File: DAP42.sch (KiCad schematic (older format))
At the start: 30 parts, among them J1 JTAG, J2 Target JTAG, J3 USB_B, Q1 AO3401, SW1 WKUP, U1 W25Q128FV, U2 STM32F042K6Tx, U3 LM1117-3.3, Y1 8MHz

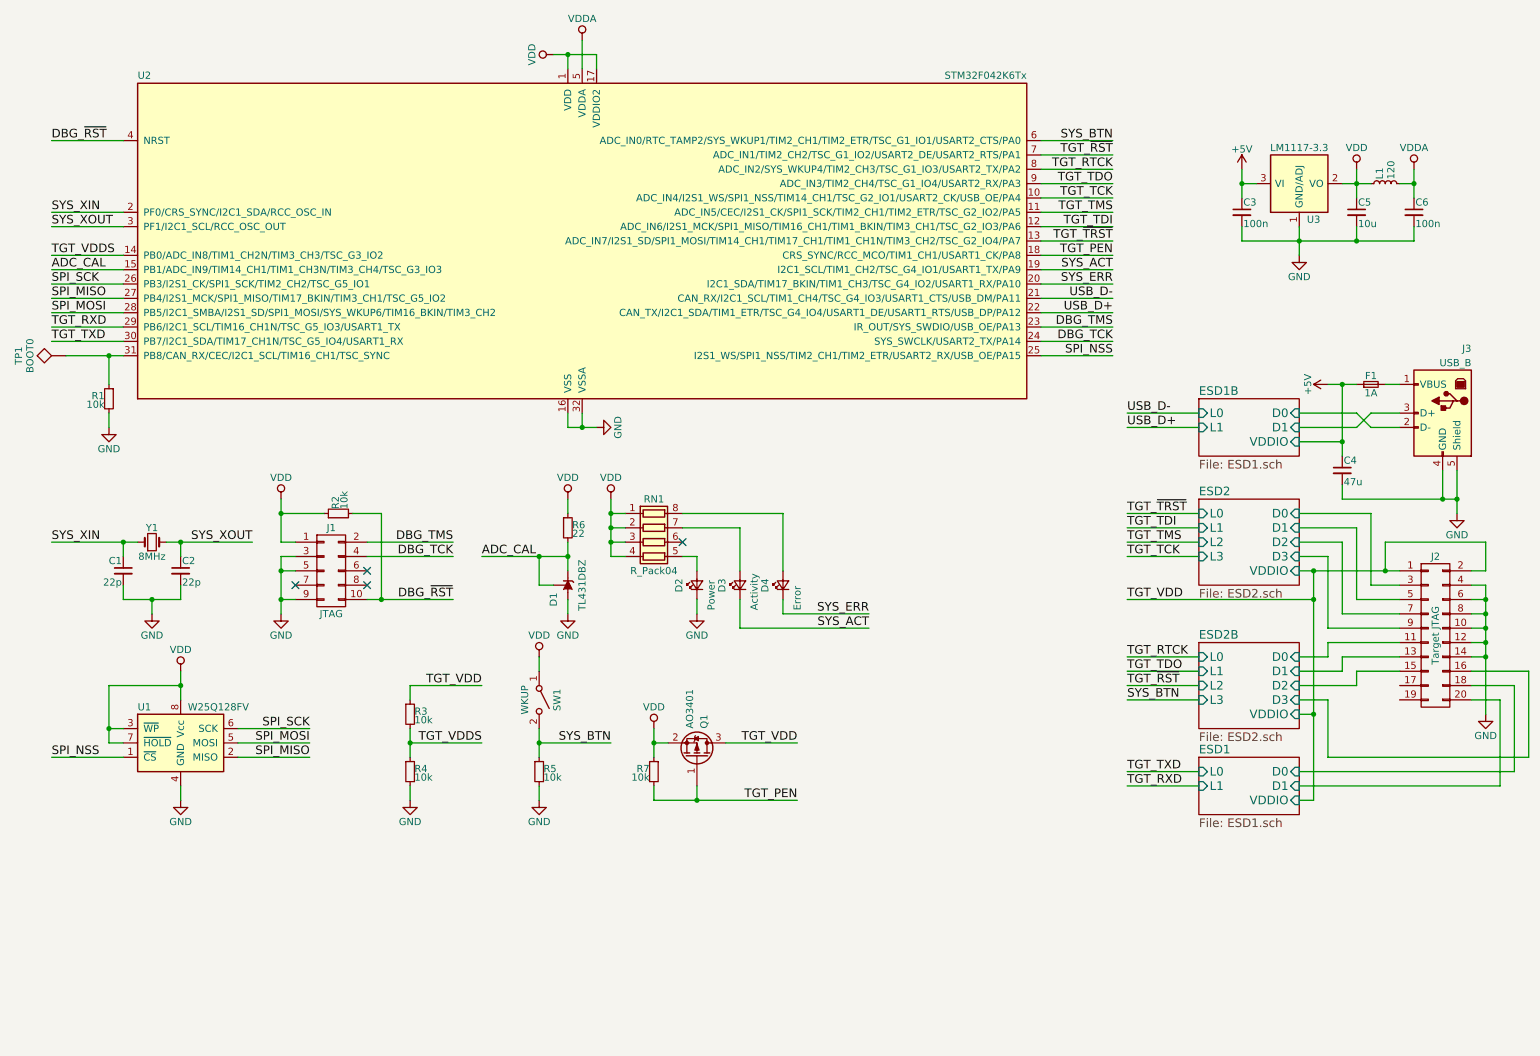
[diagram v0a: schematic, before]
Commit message: Changing the power delivery subsystem.
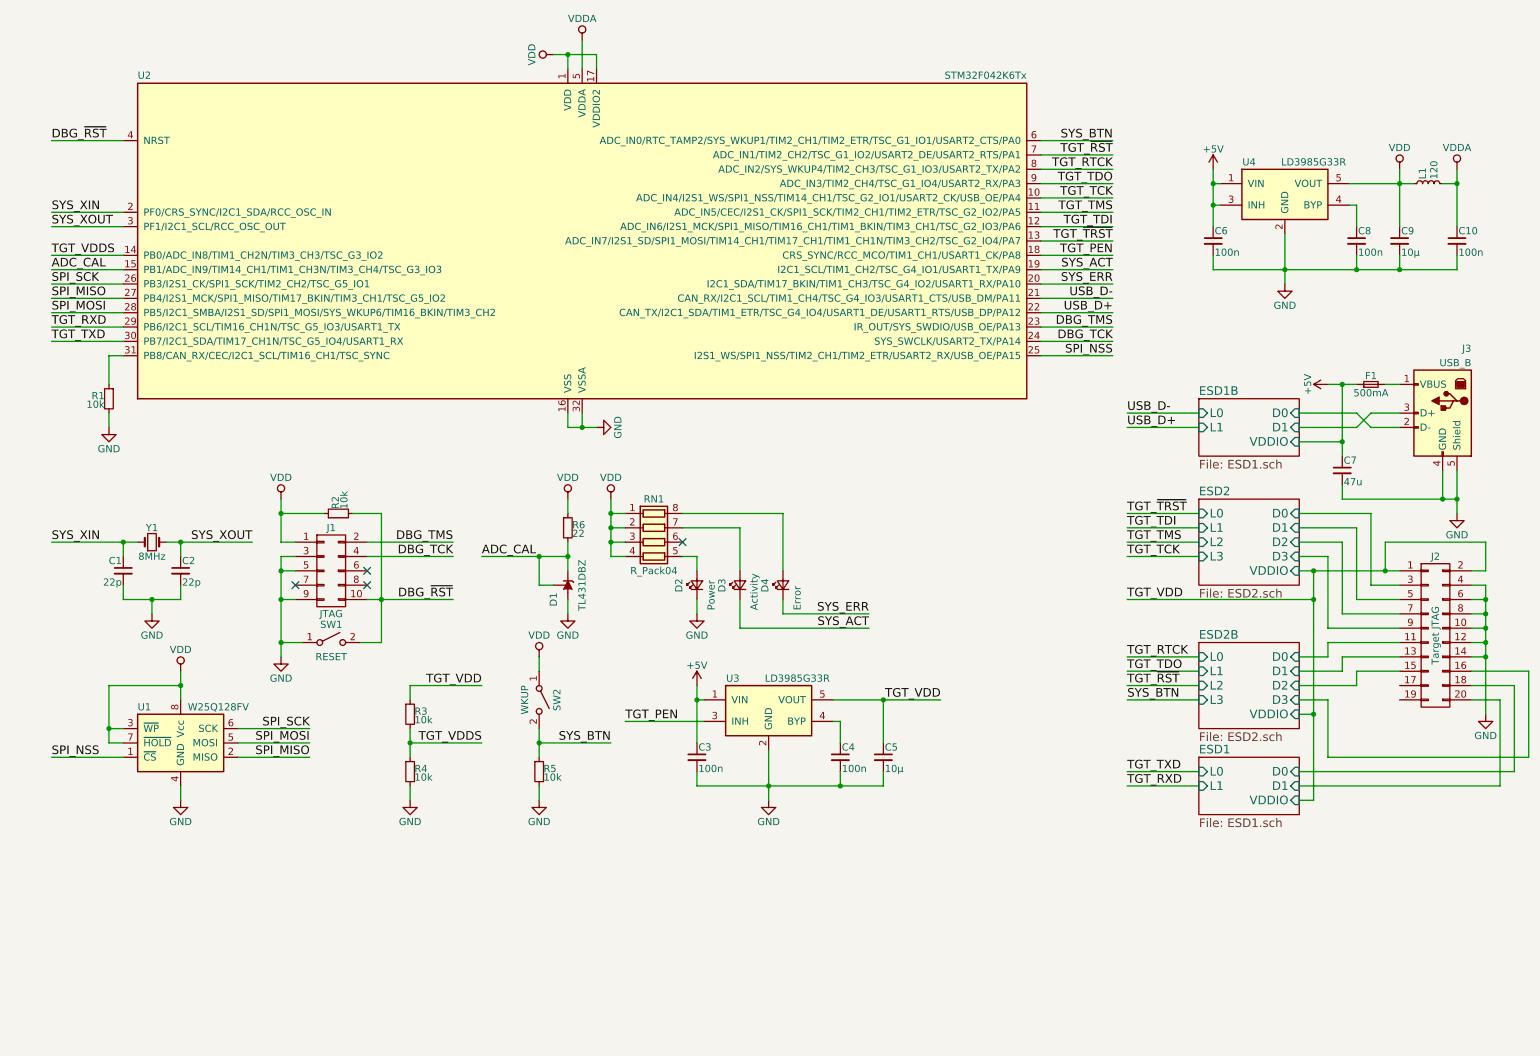
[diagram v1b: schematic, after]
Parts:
- removed Q1: AO3401, TO_SOT_Packages_SMD:SOT-23_Handsoldering, symbol Q_PMOS_GSD
- removed R7: 10k, Resistors_SMD:R_0603_HandSoldering, symbol R_Small
- removed TP1: BOOT0, SMD_Packages:1Pin, symbol TEST
- removed U3: LM1117-3.3, TO_SOT_Packages_SMD:SOT-223, symbol LM1117-3.3
- added C3, C4, C8: 100n, Capacitors_SMD:C_0603_HandSoldering, symbol C_Small
- added C5: 10µ, Capacitors_SMD:C_0805_HandSoldering, symbol C_Small
- added SW1: RESET, Buttons_Switches_SMD:SW_SPST_FSMSM, symbol SW_SPST
- added U3, U4: LD3985G33R, TO_SOT_Packages_SMD:TSOT-23-5_HandSoldering, symbol LD3985G33R
- C9: renamed from C5; value 10u -> 10µ
- F1: value 1A -> 500mA; footprint Resistors_SMD:R_1206_HandSoldering -> Resistors_SMD:R_0805_HandSoldering
- renumbered C6 to C10, C3 to C6, C4 to C7, SW1 to SW2
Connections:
- net +5V: now also C3.1, U3.1 (VIN), U4.1 (VIN), U4.3 (INH)
- net DBG_~RST: now also SW1.2 (B)
- net GND: now also C3.2, C4.2, C5.2, C8.2, SW1.1 (A), U3.2 (GND), U4.2 (GND)
- net TGT_PEN: now also U3.3 (INH)
- net TGT_VDD: now also C5.1, U3.5 (VOUT)
- net VDD: now also U4.5 (VOUT)
- new net: C8.1, U4.4 (BYP)
- new net: C4.1, U3.4 (BYP)
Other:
- moved on the sheet: C10, C6, C9, L1

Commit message: STM32F1 branch: creating a F103 mockup
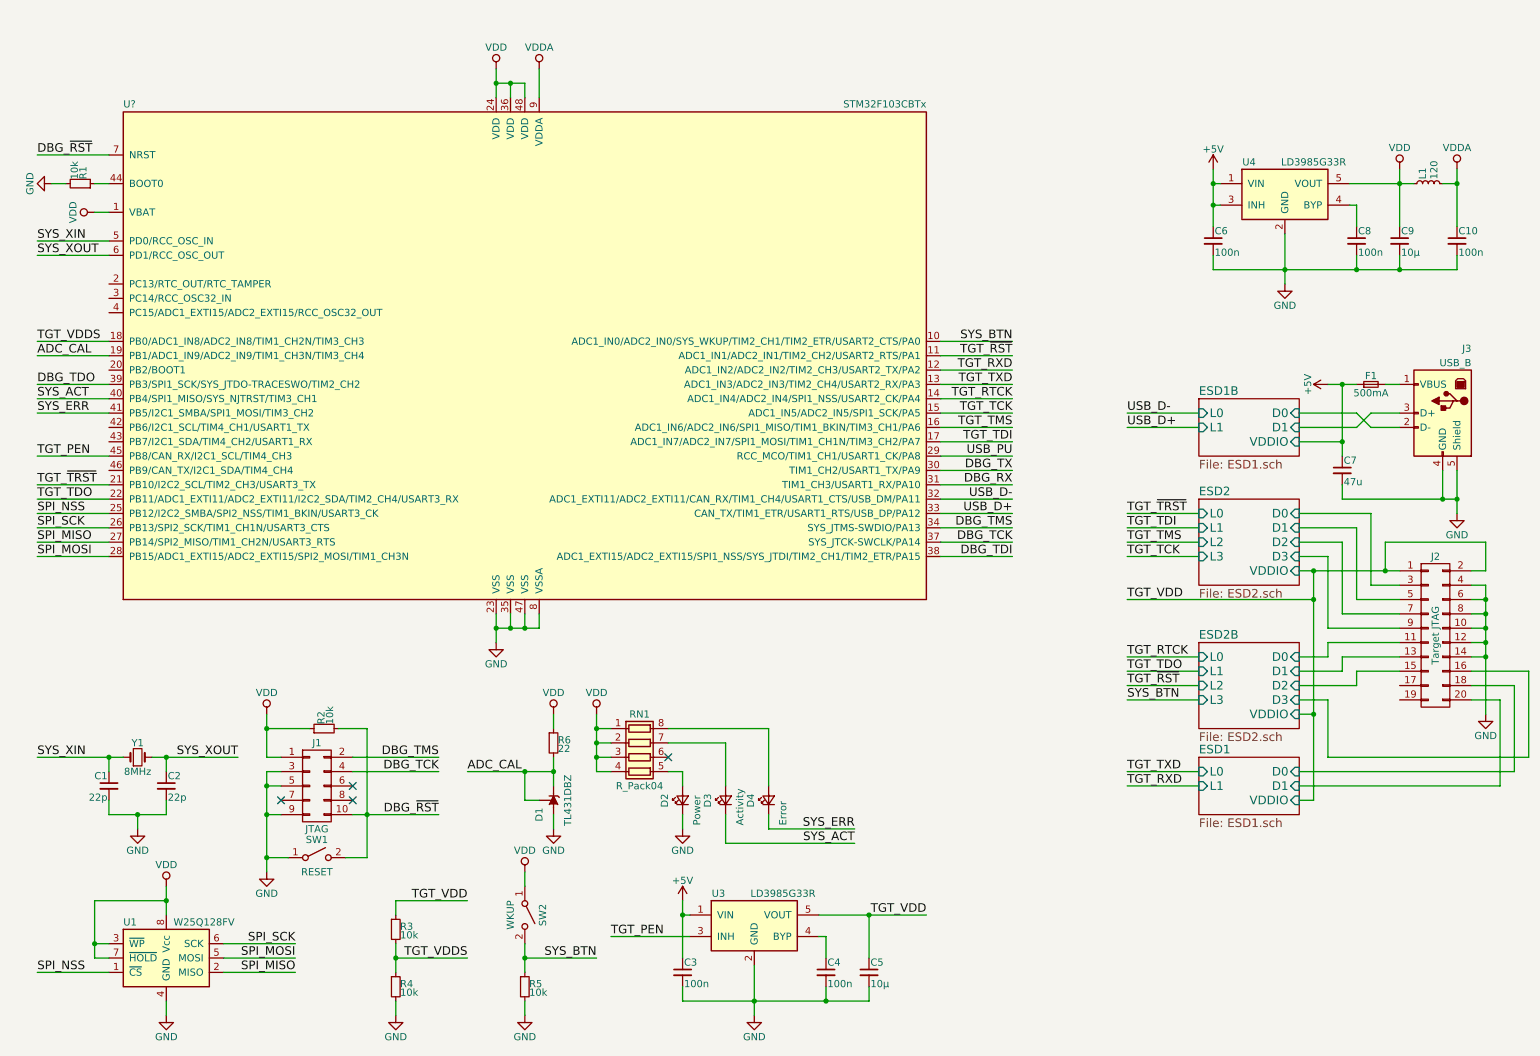
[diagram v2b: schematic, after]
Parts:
- removed U2: STM32F042K6Tx, Housings_QFP:LQFP-32_7x7mm_Pitch0.8mm, symbol STM32F042K6Tx
- added U?: STM32F103CBTx, Housings_QFP:LQFP-48_7x7mm_Pitch0.5mm, symbol STM32F103CBTx
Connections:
- net ADC_CAL: now also U?.19 (PB1/ADC1_IN9/ADC2_IN9/TIM1_CH3N/TIM3_CH4)
- net DBG_TCK: now also U?.37 (SYS_JTCK-SWCLK/PA14)
- net DBG_TMS: now also U?.34 (SYS_JTMS-SWDIO/PA13)
- net DBG_~RST: now also U?.7 (NRST)
- net GND: now also U?.23 (VSS), U?.35 (VSS), U?.47 (VSS), U?.8 (VSSA)
- net SPI_MISO: now also U?.27 (PB14/SPI2_MISO/TIM1_CH2N/USART3_RTS)
- net SPI_MOSI: now also U?.28 (PB15/ADC1_EXTI15/ADC2_EXTI15/SPI2_MOSI/TIM1_CH3N)
- net SPI_NSS: now also U?.25 (PB12/I2C2_SMBA/SPI2_NSS/TIM1_BKIN/USART3_CK)
- net SPI_SCK: now also U?.26 (PB13/SPI2_SCK/TIM1_CH1N/USART3_CTS)
- net SYS_ACT: now also U?.40 (PB4/SPI1_MISO/SYS_NJTRST/TIM3_CH1)
- net SYS_BTN: now also U?.10 (ADC1_IN0/ADC2_IN0/SYS_WKUP/TIM2_CH1/TIM2_ETR/USART2_CTS/PA0)
- net SYS_ERR: now also U?.41 (PB5/I2C1_SMBA/SPI1_MOSI/TIM3_CH2)
- net SYS_XIN: now also U?.5 (PD0/RCC_OSC_IN)
- net SYS_XOUT: now also U?.6 (PD1/RCC_OSC_OUT)
- net TGT_PEN: now also U?.45 (PB8/CAN_RX/I2C1_SCL/TIM4_CH3)
- net TGT_RTCK: now also U?.14 (ADC1_IN4/ADC2_IN4/SPI1_NSS/USART2_CK/PA4)
- net TGT_RXD: now also U?.12 (ADC1_IN2/ADC2_IN2/TIM2_CH3/USART2_TX/PA2)
- net TGT_TCK: now also U?.15 (ADC1_IN5/ADC2_IN5/SPI1_SCK/PA5)
- net TGT_TDI: now also U?.17 (ADC1_IN7/ADC2_IN7/SPI1_MOSI/TIM1_CH1N/TIM3_CH2/PA7)
- net TGT_TDO: now also U?.22 (PB11/ADC1_EXTI11/ADC2_EXTI11/I2C2_SDA/TIM2_CH4/USART3_RX)
- net TGT_TMS: now also U?.16 (ADC1_IN6/ADC2_IN6/SPI1_MISO/TIM1_BKIN/TIM3_CH1/PA6)
- net TGT_TXD: now also U?.13 (ADC1_IN3/ADC2_IN3/TIM2_CH4/USART2_RX/PA3)
- net TGT_VDDS: now also U?.18 (PB0/ADC1_IN8/ADC2_IN8/TIM1_CH2N/TIM3_CH3)
- net TGT_~RST: now also U?.11 (ADC1_IN1/ADC2_IN1/TIM2_CH2/USART2_RTS/PA1)
- net TGT_~TRST: now also U?.21 (PB10/I2C2_SCL/TIM2_CH3/USART3_TX)
- net USB_D+: now also U?.33 (CAN_TX/TIM1_ETR/USART1_RTS/USB_DP/PA12)
- net USB_D-: now also U?.32 (ADC1_EXTI11/ADC2_EXTI11/CAN_RX/TIM1_CH4/USART1_CTS/USB_DM/PA11)
- net VDD: now also U?.1 (VBAT), U?.24 (VDD), U?.36 (VDD), U?.48 (VDD)
- net VDDA: now also U?.9 (VDDA)
- net at R1.1: now also U?.44 (BOOT0)
- new net DBG_RX: U?.31 (TIM1_CH3/USART1_RX/PA10)
- new net DBG_TDI: U?.38 (ADC1_EXTI15/ADC2_EXTI15/SPI1_NSS/SYS_JTDI/TIM2_CH1/TIM2_ETR/PA15)
- new net DBG_TDO: U?.39 (PB3/SPI1_SCK/SYS_JTDO-TRACESWO/TIM2_CH2)
- new net DBG_TX: U?.30 (TIM1_CH2/USART1_TX/PA9)
- new net USB_PU: U?.29 (RCC_MCO/TIM1_CH1/USART1_CK/PA8)
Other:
- moved on the sheet: C1, C2, C3, C4, C5, D1, D2, D3, D4, J1, R1, R2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
